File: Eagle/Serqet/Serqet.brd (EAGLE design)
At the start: 127 x 43.2 mm, 65 parts

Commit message: Inverted bit order between ADC and FPGA for better layout
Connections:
- net ADC_OUT_0: now also FPGA.PIN_47; no longer FPGA.PIN_27
- net ADC_OUT_1: now also FPGA.PIN_41; no longer FPGA.PIN_34
- net ADC_OUT_2: now also FPGA.PIN_38; no longer FPGA.PIN_35
- net ADC_OUT_3: now also FPGA.PIN_37; no longer FPGA.PIN_36
- net ADC_OUT_4: now also FPGA.PIN_36; no longer FPGA.PIN_37
- net ADC_OUT_5: now also FPGA.PIN_35; no longer FPGA.PIN_38
- net ADC_OUT_6: now also FPGA.PIN_34; no longer FPGA.PIN_41
- net ADC_OUT_7: now also FPGA.PIN_27; no longer FPGA.PIN_47
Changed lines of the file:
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@@
 </signal>
 <signal name="ADC_OUT_0">
-<contactref element="FPGA" pad="PIN_27"/>
 <contactref element="ADC" pad="20"/>
-<wire x1="-39.37" y1="34.29" x2="-98.175" y2="88.715" width="0" layer="19" extent="1-1"/>
+<contactref element="FPGA" pad="PIN_47"/>
+<wire x1="-98.175" y1="88.715" x2="-39.37" y2="16.51" width="0" layer="19" extent="1-1"/>
 </signal>
 <signal name="ADC_OUT_1">
-<contactref element="FPGA" pad="PIN_34"/>
 <contactref element="ADC" pad="19"/>
-<wire x1="-39.37" y1="31.75" x2="-97.525" y2="88.715" width="0" layer="19" extent="1-1"/>
+<contactref element="FPGA" pad="PIN_41"/>
+<wire x1="-97.525" y1="88.715" x2="-39.37" y2="19.05" width="0" layer="19" extent="1-1"/>
 </signal>
 <signal name="ADC_OUT_2">
-<contactref element="FPGA" pad="PIN_35"/>
 <contactref element="ADC" pad="18"/>
-<wire x1="-96.875" y1="88.715" x2="-39.37" y2="29.21" width="0" layer="19" extent="1-1"/>
+<contactref element="FPGA" pad="PIN_38"/>
+<wire x1="-96.875" y1="88.715" x2="-39.37" y2="21.59" width="0" layer="19" extent="1-1"/>
 </signal>
 <signal name="ADC_OUT_4">
-<contactref element="FPGA" pad="PIN_37"/>
 <contactref element="ADC" pad="14"/>
-<wire x1="-94.275" y1="88.715" x2="-39.37" y2="24.13" width="0" layer="19" extent="1-1"/>
+<contactref element="FPGA" pad="PIN_36"/>
+<wire x1="-94.275" y1="88.715" x2="-39.37" y2="26.67" width="0" layer="19" extent="1-1"/>
 </signal>
 <signal name="ADC_OUT_5">
-<contactref element="FPGA" pad="PIN_38"/>
 <contactref element="ADC" pad="13"/>
-<wire x1="-93.625" y1="88.715" x2="-39.37" y2="21.59" width="0" layer="19" extent="1-1"/>
+<contactref element="FPGA" pad="PIN_35"/>
+<wire x1="-93.625" y1="88.715" x2="-39.37" y2="29.21" width="0" layer="19" extent="1-1"/>
 </signal>
 <signal name="ADC_OUT_6">
-<contactref element="FPGA" pad="PIN_41"/>
 <contactref element="ADC" pad="12"/>
-<wire x1="-92.975" y1="88.715" x2="-39.37" y2="19.05" width="0" layer="19" extent="1-1"/>
+<contactref element="FPGA" pad="PIN_34"/>
+<wire x1="-92.975" y1="88.715" x2="-39.37" y2="31.75" width="0" layer="19" extent="1-1"/>
 </signal>
 <signal name="ADC_OUT_7">
-<contactref element="FPGA" pad="PIN_47"/>
 <contactref element="ADC" pad="11"/>
-<wire x1="-92.325" y1="88.715" x2="-39.37" y2="16.51" width="0" layer="19" extent="1-1"/>
+<contactref element="FPGA" pad="PIN_27"/>
+<wire x1="-39.37" y1="34.29" x2="-92.325" y2="88.715" width="0" layer="19" extent="1-1"/>
 </signal>
 <signal name="ADC_OUT_3">
-<contactref element="FPGA" pad="PIN_36"/>
 <contactref element="ADC" pad="17"/>
-<wire x1="-96.225" y1="88.715" x2="-39.37" y2="26.67" width="0" layer="19" extent="1-1"/>
+<contactref element="FPGA" pad="PIN_37"/>
+<wire x1="-96.225" y1="88.715" x2="-39.37" y2="24.13" width="0" layer="19" extent="1-1"/>
 </signal>
 <signal name="ADC_ENCODE">

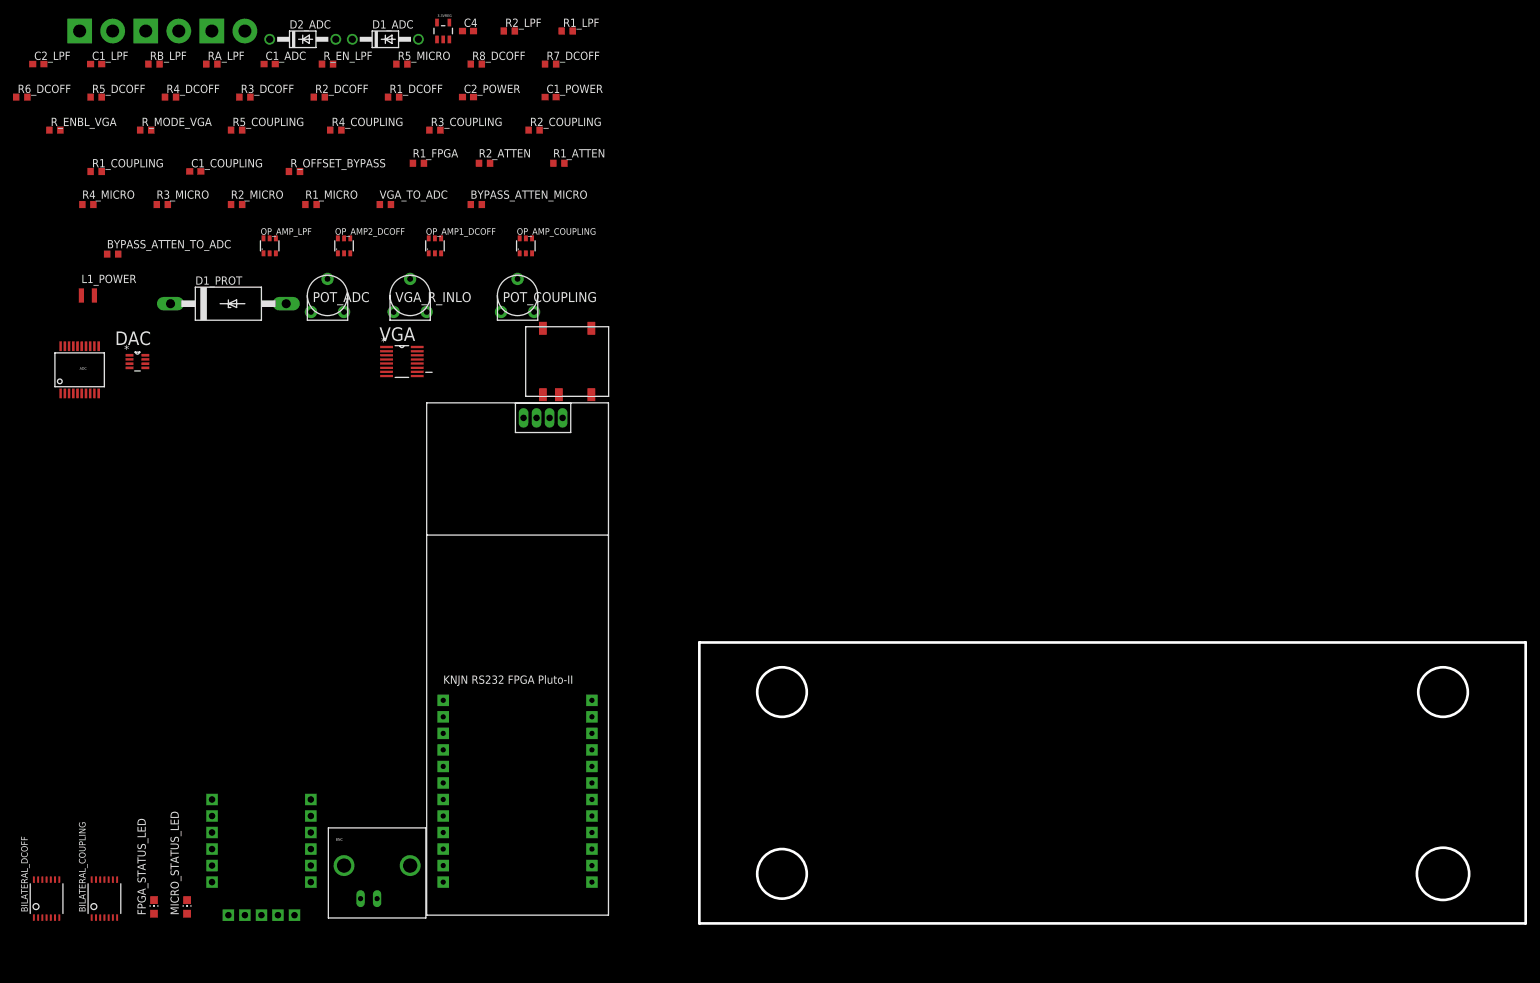
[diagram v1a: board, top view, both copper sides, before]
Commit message: Started Placing parts
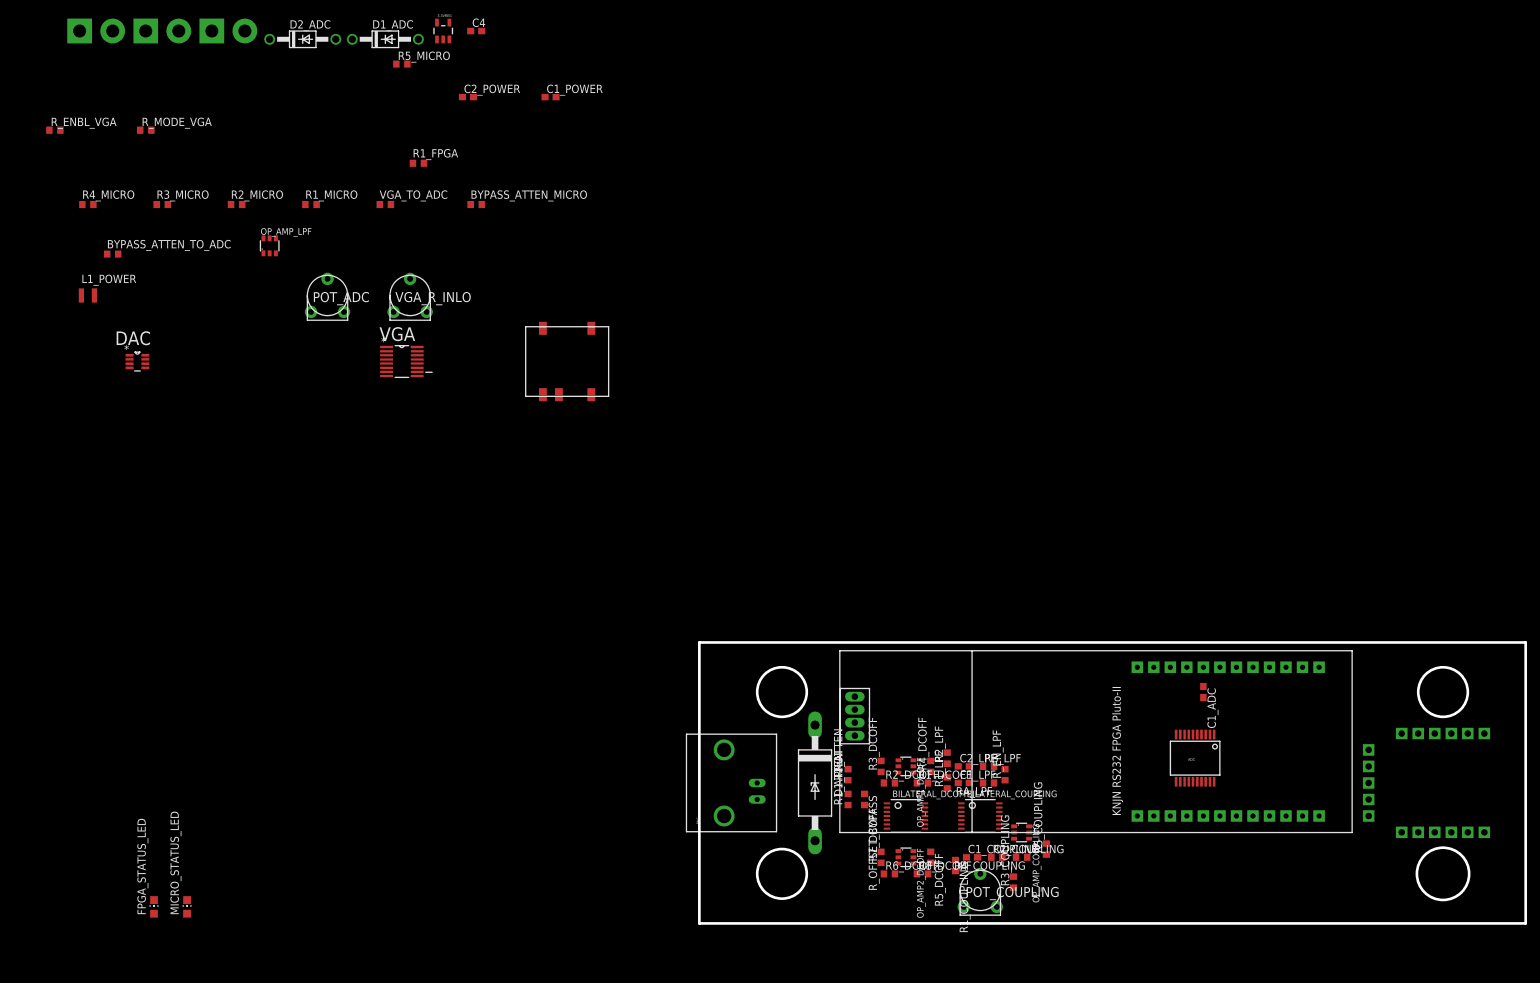
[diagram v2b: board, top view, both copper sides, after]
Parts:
- moved MICRO 183.0 mm to (115.6, 21.6), turned to 270 degrees
- moved ADC 181.5 mm to (76.2, 25.4), turned to 180 degrees
- moved R6_DCOFF 179.0 mm to (29.2, 7.62)
- moved C2_LPF 178.6 mm to (40.6, 24.1)
- moved R5_DCOFF 173.5 mm to (35.6, 10.2), turned to 270 degrees
- moved C1_LPF 173.2 mm to (40.6, 21.6)
- moved C1_ADC 172.9 mm to (77.5, 35.6), turned to 270 degrees
- moved R1_COUPLING 169.8 mm to (39.4, 8.89), turned to 270 degrees
- moved RB_LPF 167.6 mm to (44.5, 24.1)
- moved R5_COUPLING 166.4 mm to (53.3, 11.4), turned to 90 degrees
- moved RA_LPF 162.7 mm to (44.5, 21.6), turned to 180 degrees
- moved C1_COUPLING 159.3 mm to (41.9, 10.2)
- moved R4_DCOFF 155.7 mm to (35.6, 24.1), turned to 90 degrees
- moved R4_COUPLING 153.6 mm to (49.5, 10.2), turned to 180 degrees
- moved R_EN_LPF 150.9 mm to (47.0, 22.9), turned to 90 degrees
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
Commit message: Inital part placement
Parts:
- moved LED_THROUGHOLE 242.7 mm to (121.9, 6.35), turned to 90 degrees
- moved PAIRING_SWITCH 236.9 mm to (121.9, 36.8), turned to 270 degrees
- moved R3_MICRO 215.4 mm to (106.7, 7.62), turned to 90 degrees
- moved R4_MICRO 210.5 mm to (99.1, 26.7)
- moved BATTERY 195.9 mm to (71.1, 3.81)
- moved L1_POWER 189.1 mm to (74.9, 11.4), turned to 180 degrees
- moved R2_MICRO 187.5 mm to (99.1, 31.8)
- moved FPGA_STATUS_LED 184.2 mm to (100.3, 7.62)
- moved MICRO_STATUS_LED 183.0 mm to (104.1, 7.62)
- moved R1_FPGA 178.3 mm to (97.8, 7.62), turned to 270 degrees
- moved R5_MICRO 177.6 mm to (99.1, 29.2)
- moved R1_MICRO 176.1 mm to (99.1, 34.3)
- moved 3.3VREG 174.4 mm to (78.7, 8.89)
- moved C2_POWER 169.8 mm to (80.0, 2.54), turned to 270 degrees
- moved R_ENBL_VGA 168.4 mm to (43.2, 31.8), turned to 270 degrees
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
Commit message: Spaced parts out
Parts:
- moved R1_MICRO 15.3 mm to (88.9, 22.9), turned to 90 degrees
- moved R1_COUPLING 13.1 mm to (27.9, 2.54), turned to 180 degrees
- moved R8_DCOFF 12.5 mm to (22.9, 2.54)
- moved R2_MICRO 10.2 mm to (94.0, 22.9), turned to 90 degrees
- moved R4_MICRO 10.2 mm to (109.2, 25.4), turned to 180 degrees
- moved R5_MICRO 9.92 mm to (105.4, 36.8), turned to 90 degrees
- moved R6_DCOFF 8.98 mm to (20.3, 6.35), turned to 270 degrees
- moved OP_AMP2_DCOFF 7.41 mm to (25.4, 6.35)
- moved R_EN_LPF 6.35 mm to (53.3, 22.9)
- moved R_ENBL_VGA 5.24 mm to (48.3, 30.5)
- moved R_MODE_VGA 5.08 mm to (48.3, 35.6)
- moved VGA 4.58 mm to (34.3, 31.8)
- moved R7_DCOFF 4.58 mm to (30.5, 6.35)
- moved BILATERAL_DCOFF 4.02 mm to (30.5, 12.7)
- moved R5_DCOFF 4.02 mm to (34.3, 6.35)
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
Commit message: More spacing, updated design rules
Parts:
- moved R1_COUPLING 12.6 mm to (36.8, 11.4)
- moved R_EN_LPF 7.62 mm to (61.0, 22.9)
- moved R_MODE_VGA 7.41 mm to (54.6, 39.4)
- moved OP_AMP_LPF 6.84 mm to (49.5, 33.0)
- moved R_ENBL_VGA 6.48 mm to (54.6, 31.8)
- moved RA_LPF 5.08 mm to (53.3, 21.6)
- moved RB_LPF 5.08 mm to (53.3, 25.4)
- moved OP_AMP_COUPLING 5.08 mm to (57.1, 16.5)
- moved C2_LPF 4.58 mm to (47.0, 27.9)
- moved R2_LPF 4.58 mm to (41.9, 27.9), turned to 0 degrees
- moved C1_LPF 4.02 mm to (47.0, 22.9)
- moved R4_DCOFF 4.02 mm to (38.1, 25.4)
- moved VGA_TO_ADC 4.02 mm to (59.7, 33.0)
- moved R1_LPF 4.02 mm to (41.9, 22.9), turned to 0 degrees
- moved R5_COUPLING 3.81 mm to (55.9, 11.4)
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
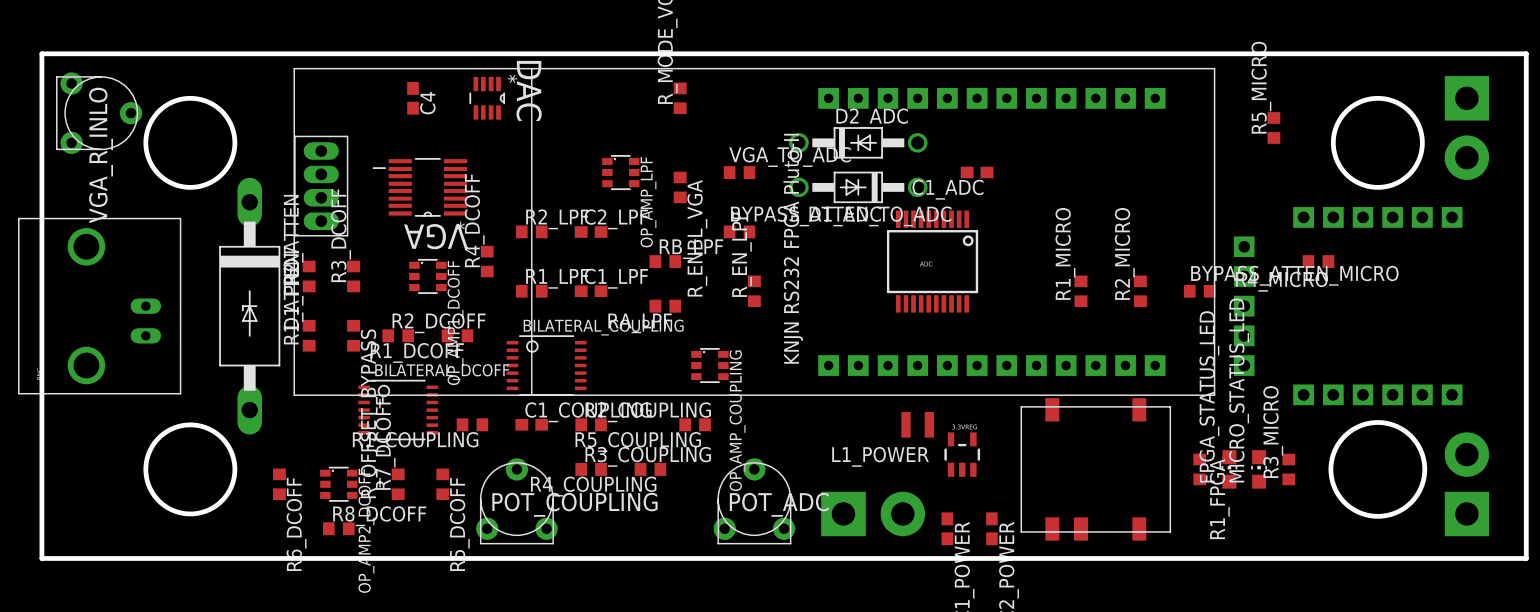
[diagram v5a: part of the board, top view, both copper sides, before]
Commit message: Updated pads to prevent routing between them.  Autorouted!
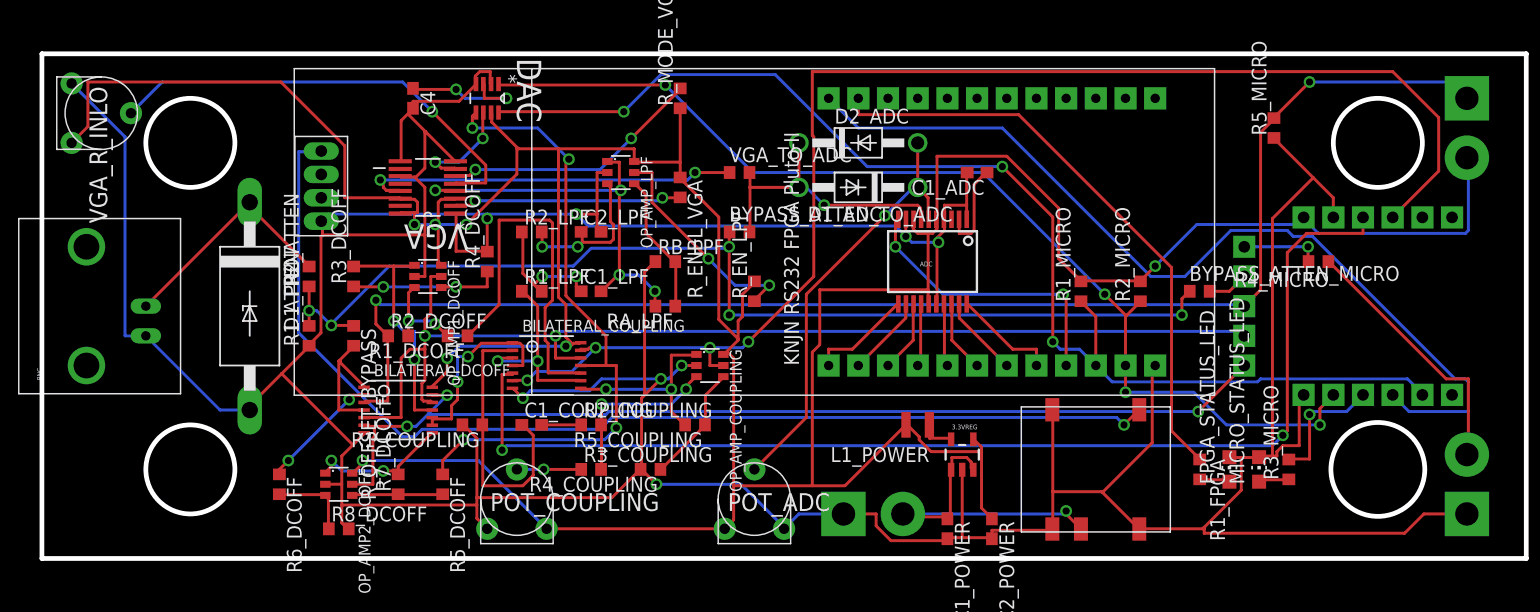
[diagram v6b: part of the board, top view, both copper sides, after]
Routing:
- net GND: track 0.00 -> 441.4 mm, vias 0 -> 8
- net VCC: track 0.00 -> 331.4 mm, vias 0 -> 7
- net N$22: track 0.00 -> 121.2 mm, vias 0 -> 2
- net AC_EN: track 0.00 -> 116.5 mm, vias 0 -> 4
- net SDA: track 0.00 -> 104.3 mm, vias 0 -> 3
- net DC_EN: track 0.00 -> 99.1 mm, vias 0 -> 2
- net POS_OFFSET_EN: track 0.00 -> 97.8 mm, vias 0 -> 2
- net 5VRAIL: track 0.00 -> 94.5 mm, vias 0 -> 1
- net ATTEN_OUT: track 0.00 -> 92.9 mm, vias 0 -> 5
- net SCL: track 0.00 -> 91.1 mm, vias 0 -> 4
- net NEG_OFFSET_EN: track 0.00 -> 87.9 mm, vias 0 -> 3
- net RESET: track 0.00 -> 77.7 mm
- net ADJ_DC_OFFSET: track 0.00 -> 55.6 mm, vias 0 -> 4
- net N$11: track 0.00 -> 51.0 mm
- net N$3: track 0.00 -> 38.6 mm, vias 0 -> 1
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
